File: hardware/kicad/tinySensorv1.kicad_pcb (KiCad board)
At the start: 2 copper layers, 94 x 60 mm, 33 parts, among them J1 RADIO, J10 CR2032 socket, J11 AAA socket, J12 AA Socket, J13 RAW IN, J2 DCDC converter, J3 I2C Sensor (BME/BMP 280), J4 PWM out, J5 OneWire sensor, J6 ISP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

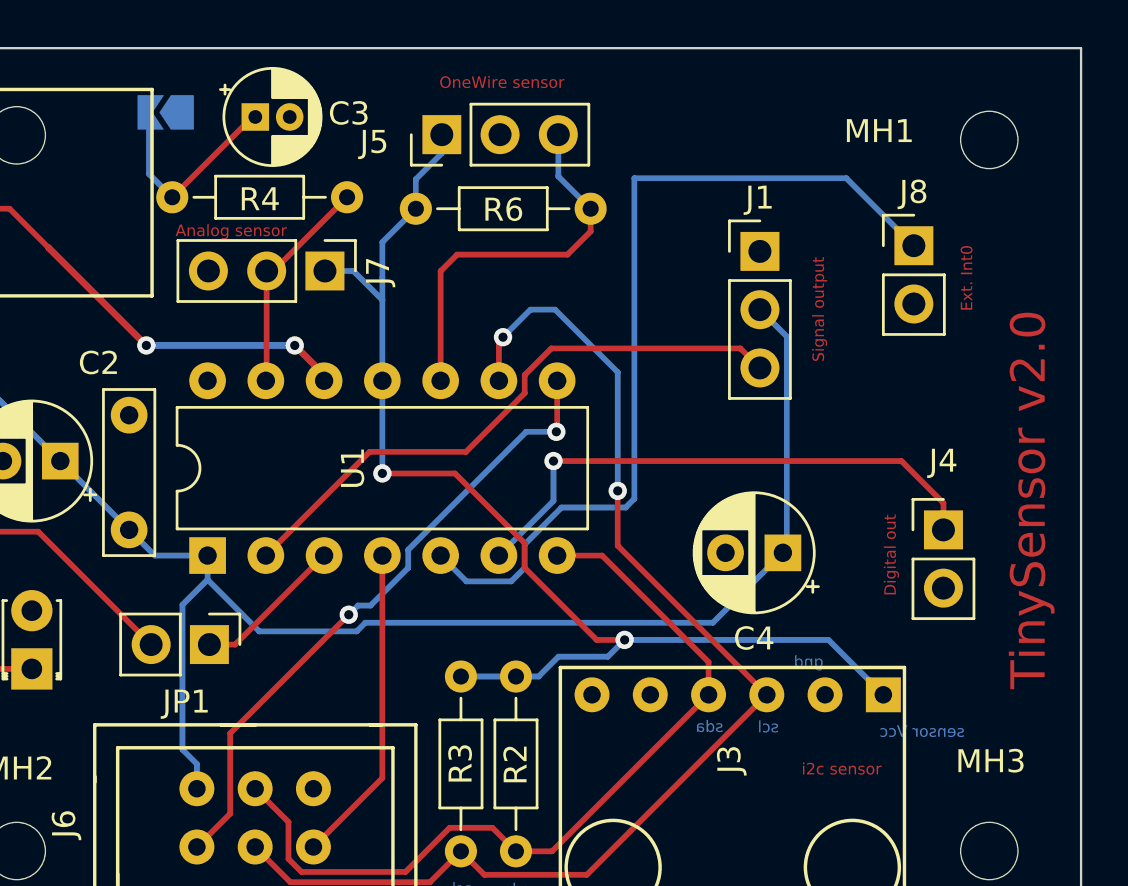
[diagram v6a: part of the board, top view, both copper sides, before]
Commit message: feat(board): Allow sub-Vss analog ref for analog sensor
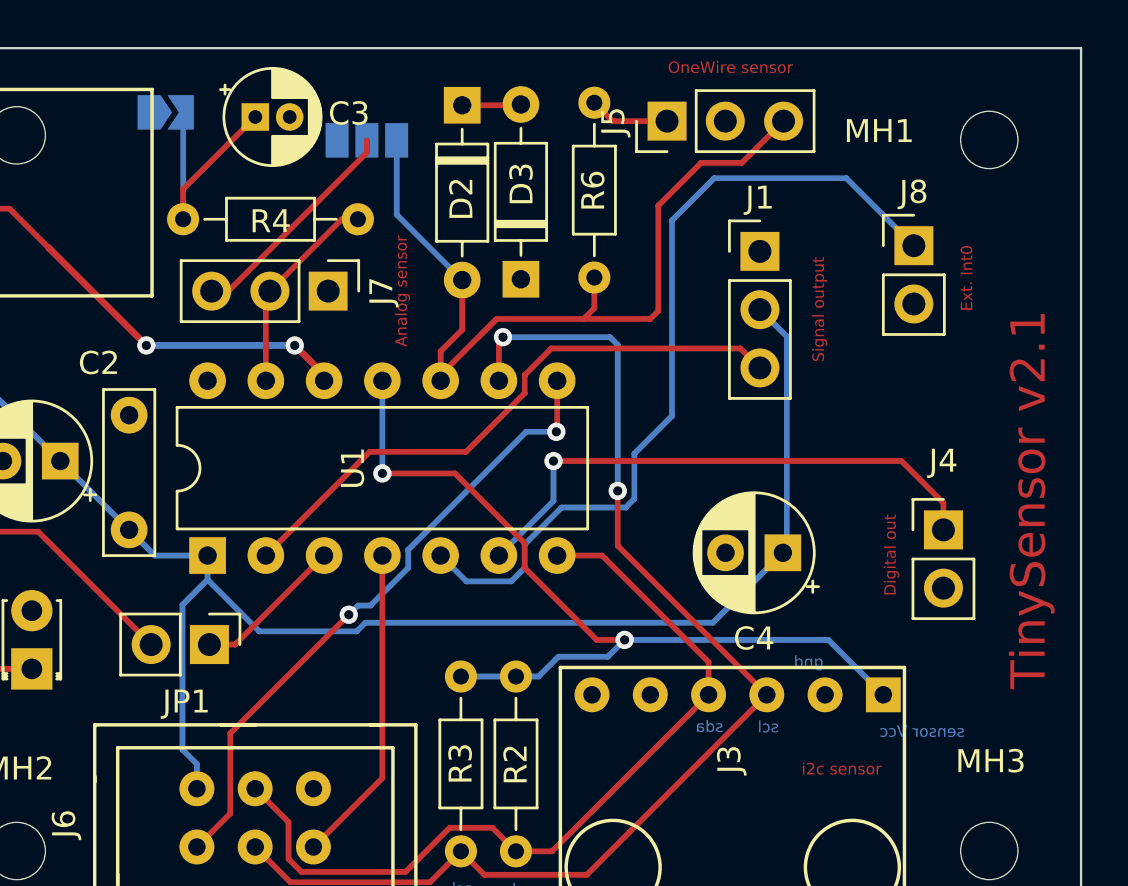
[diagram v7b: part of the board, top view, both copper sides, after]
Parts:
- added D2: 1N914, Diode_THT:D_DO-35_SOD27_P7.62mm_Horizontal, F.Cu at (180.0, 50.5)
- added D3: 1N914, Diode_THT:D_DO-35_SOD27_P7.62mm_Horizontal, F.Cu at (182.6, 58.1)
- added JP4: Analog ref, Jumper:SolderJumper-3_P1.3mm_Open_Pad1.0x1.5mm_NumberLabels, B.Cu at (175.9, 52.0)
- moved J5 9.84 mm to (189.0, 51.2)
- moved R6 8.34 mm to (185.8, 58.0), turned to 90 degrees
- moved R4 1.07 mm to (175.5, 55.5)
- moved J7 0.89 mm to (174.2, 58.6)
- turned JP3 to 0 degrees
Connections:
- J7 pad 3: GND -> Net-(J7-Pad3)
- R6 pad 1: /SENSOR_VCC -> /OneWire
- R6 pad 2: /OneWire -> /SENSOR_VCC
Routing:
- net /OneWire: track 16.8 -> 37.4 mm
- net /SENSOR_VCC: track 53.2 -> 42.1 mm
- net Net-(J7-Pad3): track 0.00 -> 9.80 mm
- net Net-(D2-Pad1): track 0.00 -> 2.63 mm
- net /INT0: track 38.4 -> 36.3 mm
- net Net-(C3-Pad1): track 9.19 -> 10.8 mm
- net /Analog_sensor: track 9.88 -> 9.17 mm
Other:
- board text added: "TinySensor v2.1"
- board text removed: "TinySensor v2.0"

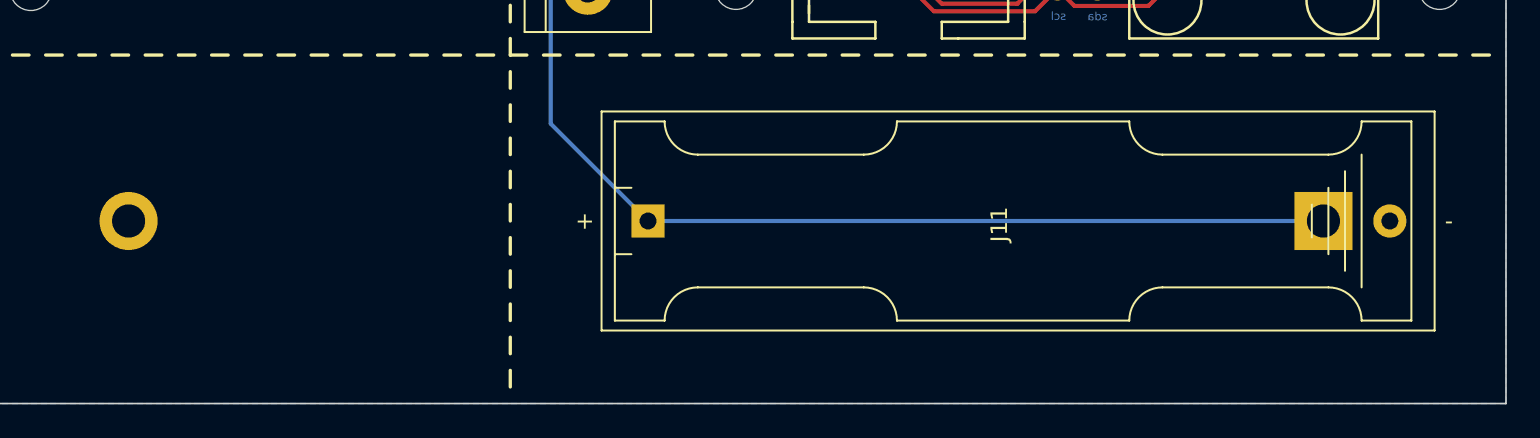
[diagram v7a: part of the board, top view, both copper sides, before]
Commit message: Fix: change AA battery footprint
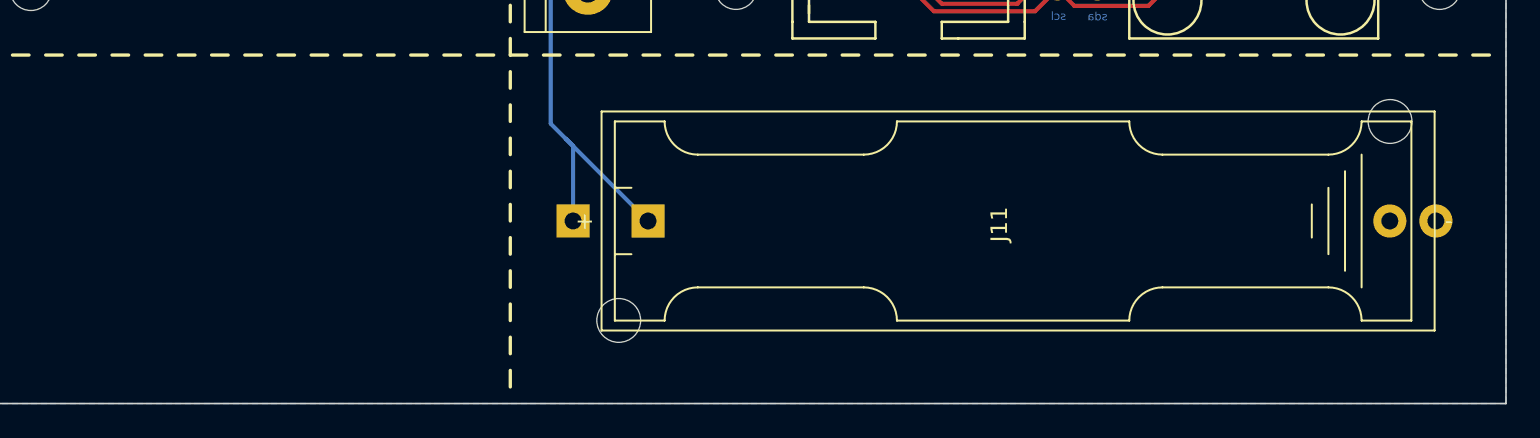
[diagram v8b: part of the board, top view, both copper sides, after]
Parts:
- J12: footprint Battery:BatteryHolder_MPD_BH-18650-PC2 -> Battery:BatteryHolder_Keystone_2460_1xAA
- moved J12 45.2 mm to (150.8, 97.0), turned to 0 degrees
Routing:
- net +BATT: track 140.9 -> 105.3 mm
